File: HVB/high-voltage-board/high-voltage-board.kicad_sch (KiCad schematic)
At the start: 10 parts, among them J1 Conn_01x23, J2 HECS, J3 HV+, J4 HV-, J5 HV+, J6 HV-, J7 Conn_01x02, J9 Bender-LV

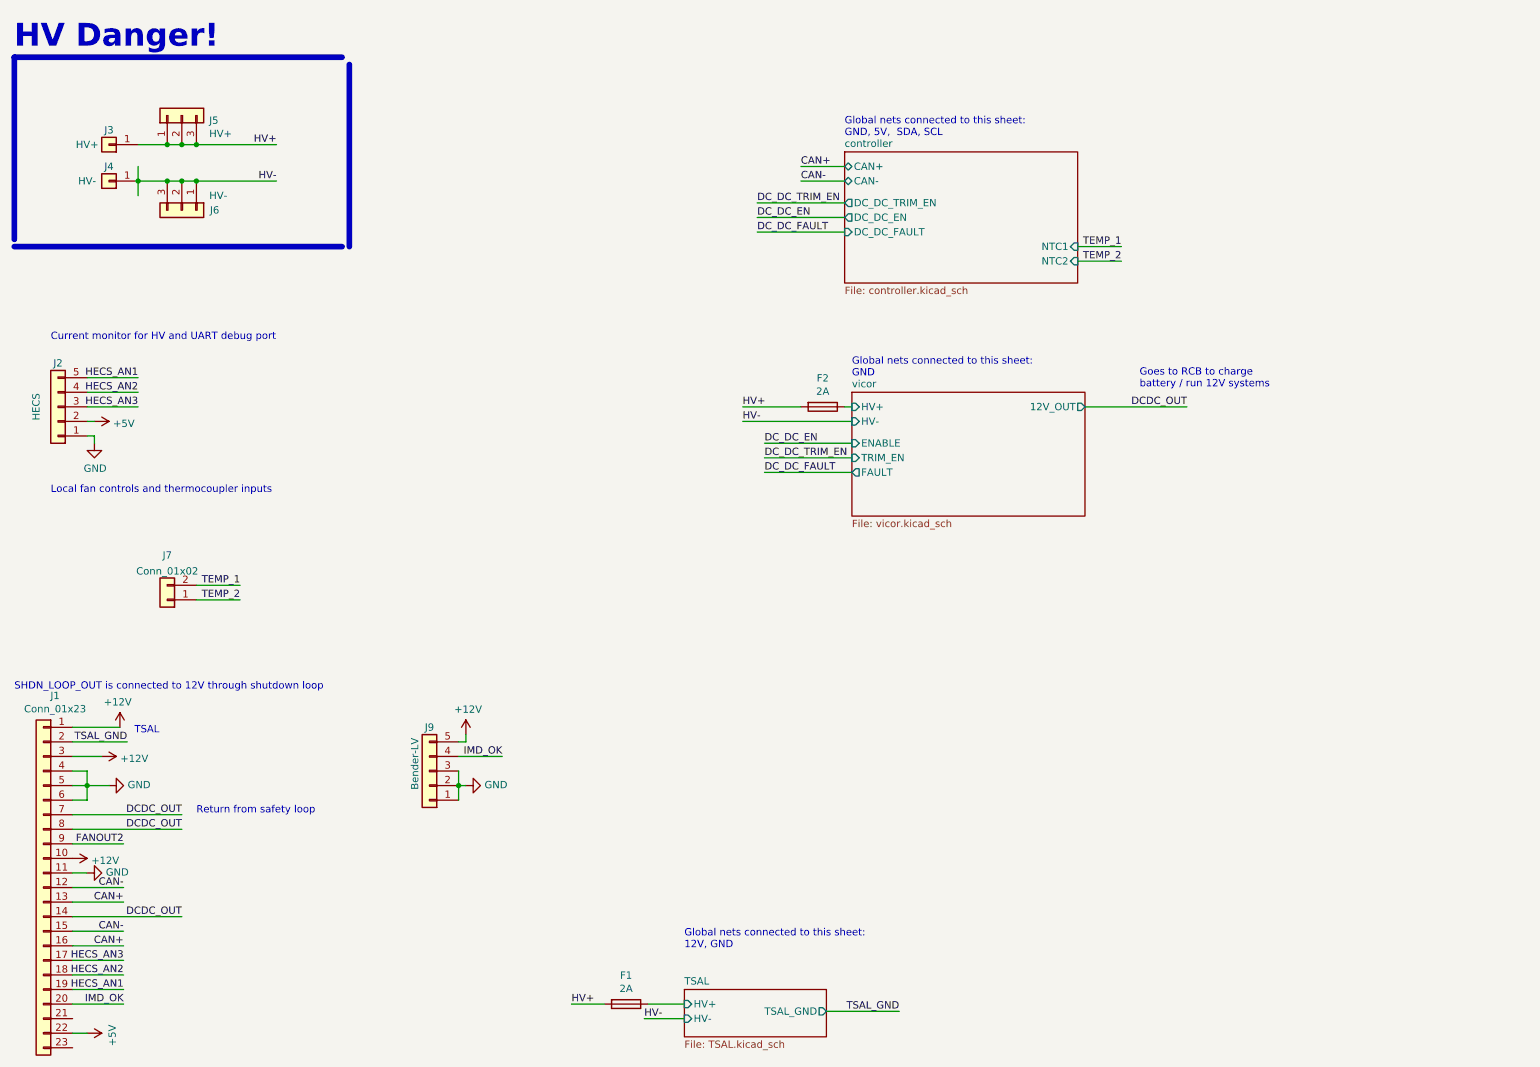
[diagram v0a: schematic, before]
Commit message: working on layout
Updating traces for RCB and organizing HVB
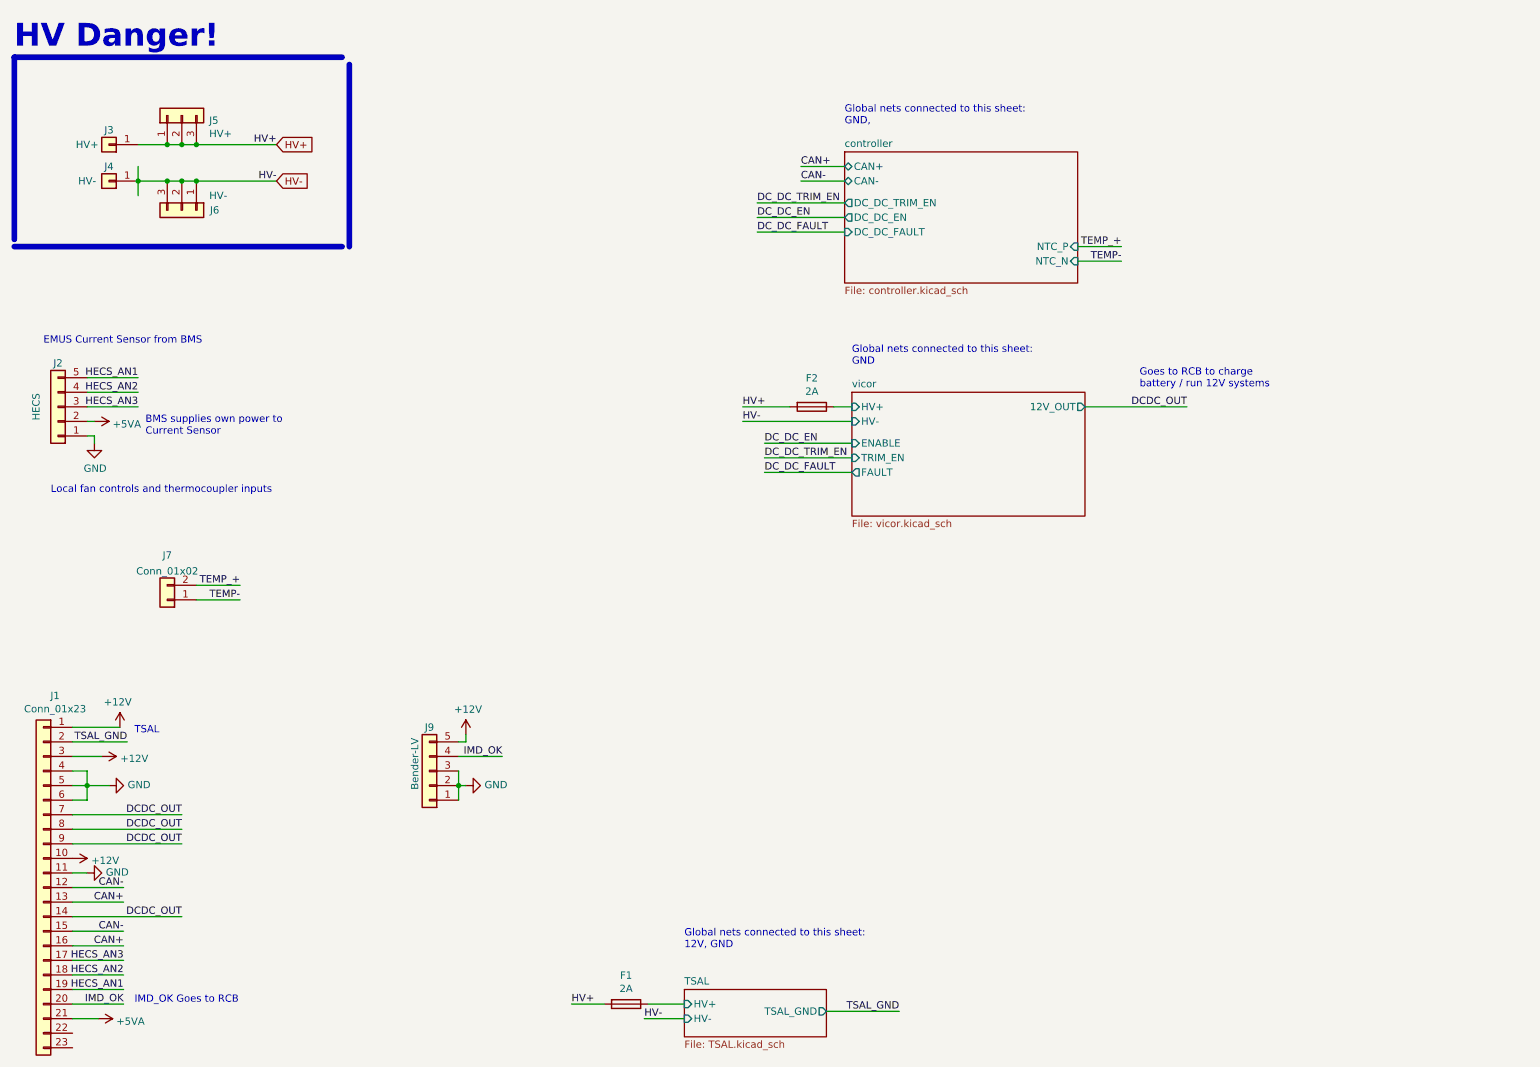
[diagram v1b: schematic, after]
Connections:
- net FANOUT2 is gone; now on net DCDC_OUT: J1.9 (Pin_9)
- net +5VA: now reaches J1.21 (Pin_21)
- net +5VA: now also J2.2 (Pin_2)
- net +5V: no longer names the net of J1.22 (Pin_22)
- net +5V: no longer J2.2 (Pin_2)
- net TEMP_1 renamed TEMP_+
- net TEMP_2 renamed TEMP-
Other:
- sheet controller ports: added NTC_N, NTC_P; removed NTC1, NTC2
- note added: "BMS supplies own power to Current Sensor"
- note added: "EMUS Current Sensor from BMS"
- note added: "Global nets connected to this sheet: GND,"
- note added: "IMD_OK Goes to RCB"
- note removed: "Current monitor for HV and UART debug port"
- note removed: "Global nets connected to this sheet: GND, 5V, SDA, SCL"
- note removed: "Return from safety loop"
- note removed: "SHDN_LOOP_OUT is connected to 12V through shutdown loop"
- moved on the sheet: F2

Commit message: updating hv layout
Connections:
- net +12V: now also J1.9 (Pin_9), J9.4 (Pin_4); no longer J1.10 (Pin_10), J1.3 (Pin_3), J9.5 (Pin_5)
- net +5VA: now also J1.15 (Pin_15); no longer J1.21 (Pin_21)
- net CAN+: no longer J1.16 (Pin_16)
- net CAN-: no longer J1.15 (Pin_15)
- net DCDC_OUT: now also J1.3 (Pin_3), J1.4 (Pin_4), J1.5 (Pin_5), J1.6 (Pin_6); no longer J1.14 (Pin_14), J1.7 (Pin_7), J1.8 (Pin_8), J1.9 (Pin_9)
- net GND: no longer J1.4 (Pin_4), J1.5 (Pin_5), J1.6 (Pin_6)
- net HECS_AN1: now also J1.17 (Pin_17); no longer J1.19 (Pin_19)
- net HECS_AN2: now also J1.10 (Pin_10); no longer J1.18 (Pin_18)
- net HECS_AN3: now also J1.18 (Pin_18); no longer J1.17 (Pin_17)
- net IMD_OK: now also J1.16 (Pin_16), J9.5 (Pin_5); no longer J1.20 (Pin_20), J9.4 (Pin_4)
- net TSAL_GND: now also J1.8 (Pin_8); no longer J1.2 (Pin_2)
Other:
- note added: "Global nets connected to this sheet: GND, 12V"
- note removed: "Global nets connected to this sheet: GND,"

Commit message: working on layout
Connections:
- net +12V: now also J1.13 (Pin_13), J1.20 (Pin_20), J1.6 (Pin_6), J1.7 (Pin_7), J9.5 (Pin_5); no longer J1.1 (Pin_1), J1.9 (Pin_9), J9.4 (Pin_4)
- net +5VA: now also J1.10 (Pin_10); no longer J1.15 (Pin_15)
- net CAN+: now also J1.14 (Pin_14), J1.15 (Pin_15); no longer J1.13 (Pin_13)
- net CAN-: now also J1.22 (Pin_22), J1.23 (Pin_23); no longer J1.12 (Pin_12)
- net DCDC_OUT: now also J1.1 (Pin_1), J1.2 (Pin_2); no longer J1.5 (Pin_5), J1.6 (Pin_6)
- net GND: now also J1.12 (Pin_12), J1.21 (Pin_21), J1.5 (Pin_5); no longer J1.11 (Pin_11)
- net HECS_AN1: now also J1.16 (Pin_16); no longer J1.17 (Pin_17)
- net HECS_AN2: now also J1.9 (Pin_9); no longer J1.10 (Pin_10)
- net HECS_AN3: now also J1.17 (Pin_17); no longer J1.18 (Pin_18)
- net IMD_OK: now also J1.18 (Pin_18), J9.4 (Pin_4); no longer J1.16 (Pin_16), J9.5 (Pin_5)
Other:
- note added: "TSAL OUTPUT Pin 7 and 8"
- note added: "Vicor temperature sensor"
- note removed: "Local fan controls and thermocoupler inputs"
- note removed: "TSAL"
- moved on the sheet: J2, J7, J9

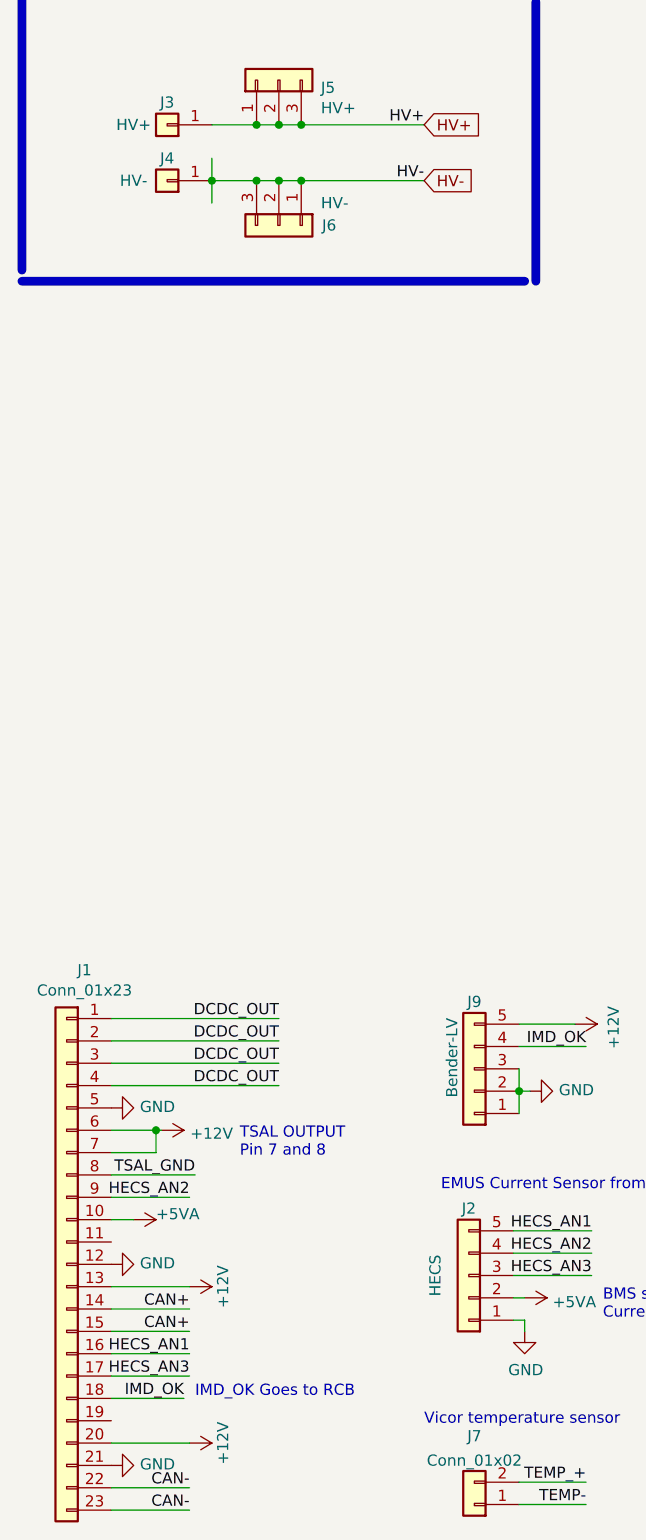
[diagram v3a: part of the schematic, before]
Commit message: almost done with layout
HV layout almost done. Tracing
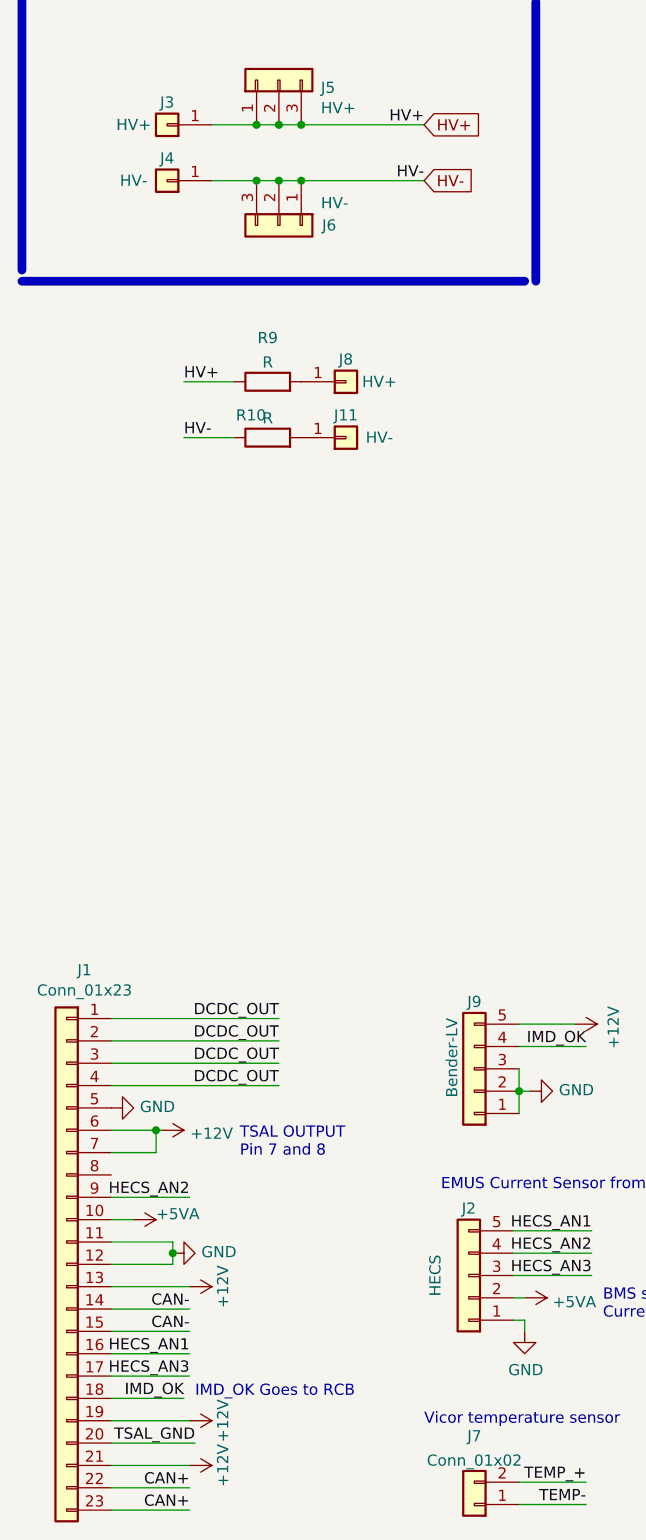
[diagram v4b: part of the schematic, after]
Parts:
- added J11: HV-, Connector_Hirose:Hirose_DF63M-1P-3.96DSA_1x01_P3.96mm_Vertical, symbol Connector_Generic:Conn_01x01
- added J8: HV+, Connector_Hirose:Hirose_DF63M-1P-3.96DSA_1x01_P3.96mm_Vertical, symbol Connector_Generic:Conn_01x01
- added R10, R9: R, Resistor_THT:R_Axial_Power_L38.0mm_W9.0mm_P45.72mm, symbol Device:R
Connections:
- net +12V: now also J1.19 (Pin_19), J1.21 (Pin_21); no longer J1.20 (Pin_20)
- net CAN+: now also J1.22 (Pin_22), J1.23 (Pin_23); no longer J1.14 (Pin_14), J1.15 (Pin_15)
- net CAN-: now also J1.14 (Pin_14), J1.15 (Pin_15); no longer J1.22 (Pin_22), J1.23 (Pin_23)
- net GND: now also J1.11 (Pin_11); no longer J1.21 (Pin_21)
- net HV+: now also R9.1
- net HV-: now also R10.1
- net TSAL_GND: now also J1.20 (Pin_20); no longer J1.8 (Pin_8)
- new net: J8.1 (Pin_1), R9.2
- new net: J11.1 (Pin_1), R10.2

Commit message: Layout Trace Complete
completed layout of tracks. Still need to place silkscreens
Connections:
- net +12V: now also J1.20 (Pin_20); no longer J1.19 (Pin_19), J1.21 (Pin_21)
- net GND: now also J1.8 (Pin_8)
- net TSAL_GND: now also J1.21 (Pin_21); no longer J1.20 (Pin_20)
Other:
- note added: "TSAL OUTPUT Pin 13 and 21"
- note removed: "TSAL OUTPUT Pin 7 and 8"
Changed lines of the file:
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@@
     (stroke (width 0) (type default) (color 0 0 0 0))
   )
-  (wire (pts (xy 26.67 189.23) (xy 35.56 189.23))
+  (wire (pts (xy 26.67 189.23) (xy 36.83 189.23))
     (stroke (width 0) (type default) (color 0 0 0 0))
   )
@@
     (stroke (width 0) (type default) (color 0 0 0 0))
   )
+  (wire (pts (xy 35.56 156.21) (xy 26.67 156.21))
+    (stroke (width 0) (type default) (color 0 0 0 0))
+  )
   (wire (pts (xy 48.26 36.83) (xy 62.23 36.83))
     (stroke (width 0) (type default) (color 0 0 0 0))
@@
     (effects (font (size 1.27 1.27)) (justify left bottom))
   )
-  (text "TSAL OUTPUT\nPin 7 and 8" (at 41.275 154.305 0)
+  (text "TSAL OUTPUT\nPin 13 and 21" (at 41.91 170.815 0)
     (effects (font (size 1.27 1.27)) (justify left bottom))
   )
@@
     (effects (font (size 1.27 1.27)) (justify right bottom))
   )
-  (label "TSAL_GND" (at 36.195 186.69 180)
+  (label "TSAL_GND" (at 36.83 189.23 180)
     (effects (font (size 1.27 1.27)) (justify right bottom))
   )
@@
     (pin "2")
   )
+  (symbol (lib_id "power:GND") (at 35.56 156.21 90) (unit 1)
+    (in_bom yes) (on_board yes)
+    (property "Reference" "#PWR0108" (id 0) (at 41.91 156.21 0)
+      (effects (font (size 1.27 1.27)) hide)
+    )
+    (property "Value" "GND" (id 1) (at 38.8112 156.083 90)
+      (effects (font (size 1.27 1.27)) (justify right))
+    )
+    (property "Footprint" "" (id 2) (at 35.56 156.21 0)
+      (effects (font (size 1.27 1.27)) hide)
+    )
+    (property "Datasheet" "" (id 3) (at 35.56 156.21 0)
+      (effects (font (size 1.27 1.27)) hide)
+    )
+    (pin "1")
+  )
   (symbol (lib_id "power:GND") (at 26.67 148.59 90) (unit 1)
     (in_bom yes) (on_board yes)
@@
     (pin "2")
   )
-  (symbol (lib_id "power:+12V") (at 35.56 189.23 270) (mirror x) (unit 1)
-    (in_bom yes) (on_board yes)
-    (property "Reference" "#PWR0108" (id 0) (at 31.75 189.23 0)
-      (effects (font (size 1.27 1.27)) hide)
-    )
-    (property "Value" "+12V" (id 1) (at 39.37 189.23 0))
-    (property "Footprint" "" (id 2) (at 35.56 189.23 0)
-      (effects (font (size 1.27 1.27)) hide)
-    )
-    (property "Datasheet" "" (id 3) (at 35.56 189.23 0)
-      (effects (font (size 1.27 1.27)) hide)
-    )
-    (pin "1")
-  )
-  (symbol (lib_id "power:+12V") (at 35.56 184.15 270) (mirror x) (unit 1)
-    (in_bom yes) (on_board yes)
-    (property "Reference" "#PWR0107" (id 0) (at 31.75 184.15 0)
-      (effects (font (size 1.27 1.27)) hide)
-    )
-    (property "Value" "+12V" (id 1) (at 39.37 184.15 0))
-    (property "Footprint" "" (id 2) (at 35.56 184.15 0)
-      (effects (font (size 1.27 1.27)) hide)
-    )
-    (property "Datasheet" "" (id 3) (at 35.56 184.15 0)
+  (symbol (lib_id "power:+12V") (at 36.195 186.69 270) (mirror x) (unit 1)
+    (in_bom yes) (on_board yes)
+    (property "Reference" "#PWR0107" (id 0) (at 32.385 186.69 0)
+      (effects (font (size 1.27 1.27)) hide)
+    )
+    (property "Value" "+12V" (id 1) (at 40.64 187.325 0))
+    (property "Footprint" "" (id 2) (at 36.195 186.69 0)
+      (effects (font (size 1.27 1.27)) hide)
+    )
+    (property "Datasheet" "" (id 3) (at 36.195 186.69 0)
       (effects (font (size 1.27 1.27)) hide)
     )
@@
       (reference "#PWR0107") (unit 1) (value "+12V") (footprint "")
     )
-    (path "/98549f14-2dde-46fe-9bbe-0196c4f77420"
-      (reference "#PWR0108") (unit 1) (value "+12V") (footprint "")
+    (path "/79cdd589-0e2f-43a0-b8f3-7a47a6bac649"
+      (reference "#PWR0108") (unit 1) (value "GND") (footprint "")
     )
     (path "/8aaed559-750b-472b-894b-2b6ccd4cd152"
@@
     )
     (path "/00000000-0000-0000-0000-00005c8304a7/00000000-0000-0000-0000-0000618b3473"
-      (reference "U5") (unit 1) (value "STM32F413CGUx") (footprint "Package_DFN_QFN:QFN-48-1EP_7x7mm_P0.5mm_EP5.3x5.3mm_ThermalVias")
+      (reference "U5") (unit 1) (value "STM32F413CGUx") (footprint "Package_DFN_QFN:QFN-48-1EP_7x7mm_P0.5mm_EP5.3x5.3mm")
     )
     (path "/00000000-0000-0000-0000-00005c8304a7/00000000-0000-0000-0000-00006198f4d7"

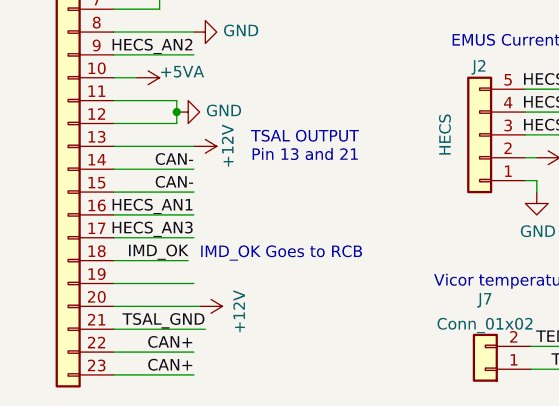
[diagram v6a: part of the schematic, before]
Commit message: updating trace correction temp
changing trace and pinout of a temp wire
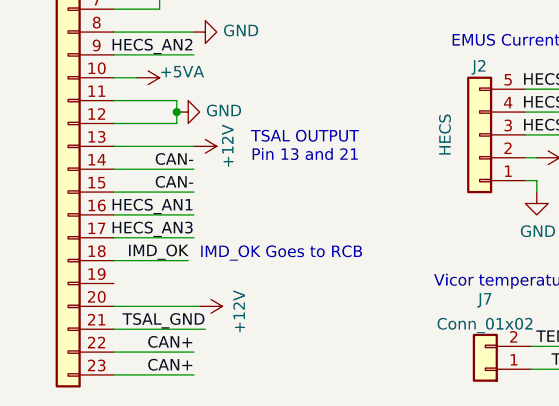
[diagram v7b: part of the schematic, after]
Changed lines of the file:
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@@
-    (stroke (width 0) (type default) (color 0 0 0 0))
-  )
-  (wire (pts (xy 26.67 184.15) (xy 35.56 184.15))
     (stroke (width 0) (type default) (color 0 0 0 0))
   )
